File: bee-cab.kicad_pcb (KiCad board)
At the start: 2 copper layers, 29 x 53.3 mm, 38 parts, among them J1 Conn_01x02_Male, J10 Conn_01x01, J11 Conn_02x01, J12 Conn_02x01, J13 Conn_01x02, J14 Conn_01x02, J15 Conn_01x02, J16 Conn_01x02, J17 Conn_01x03, J18 Conn_01x02, J19 Conn_01x02, J2 Conn_01x02_Male, J3 Conn_01x02_Male, J4 Conn_01x02_Male, J5 Conn_01x03, J6 Conn_02x03_Odd_Even, J7 Conn_02x01, J8 Conn_01x02, J9 Conn_01x02

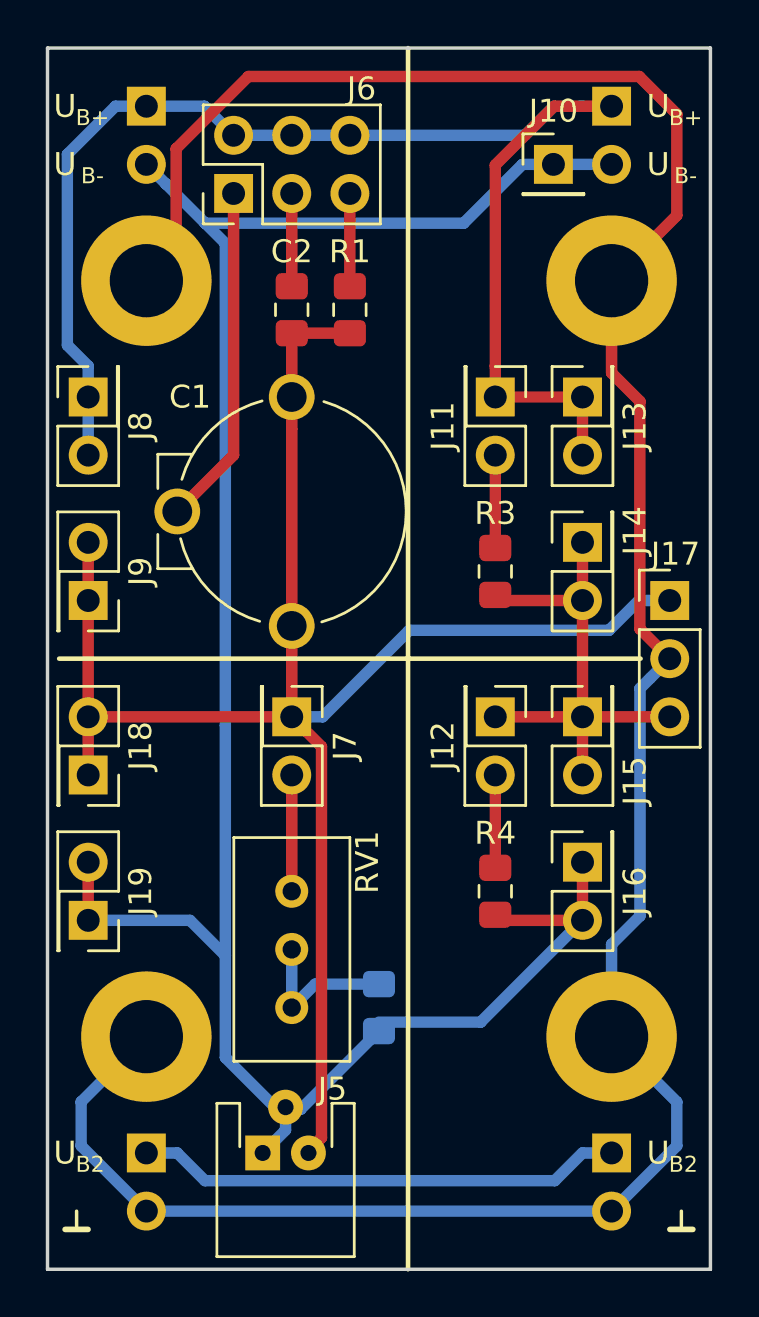
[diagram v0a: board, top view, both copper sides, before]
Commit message: Add text and logos.
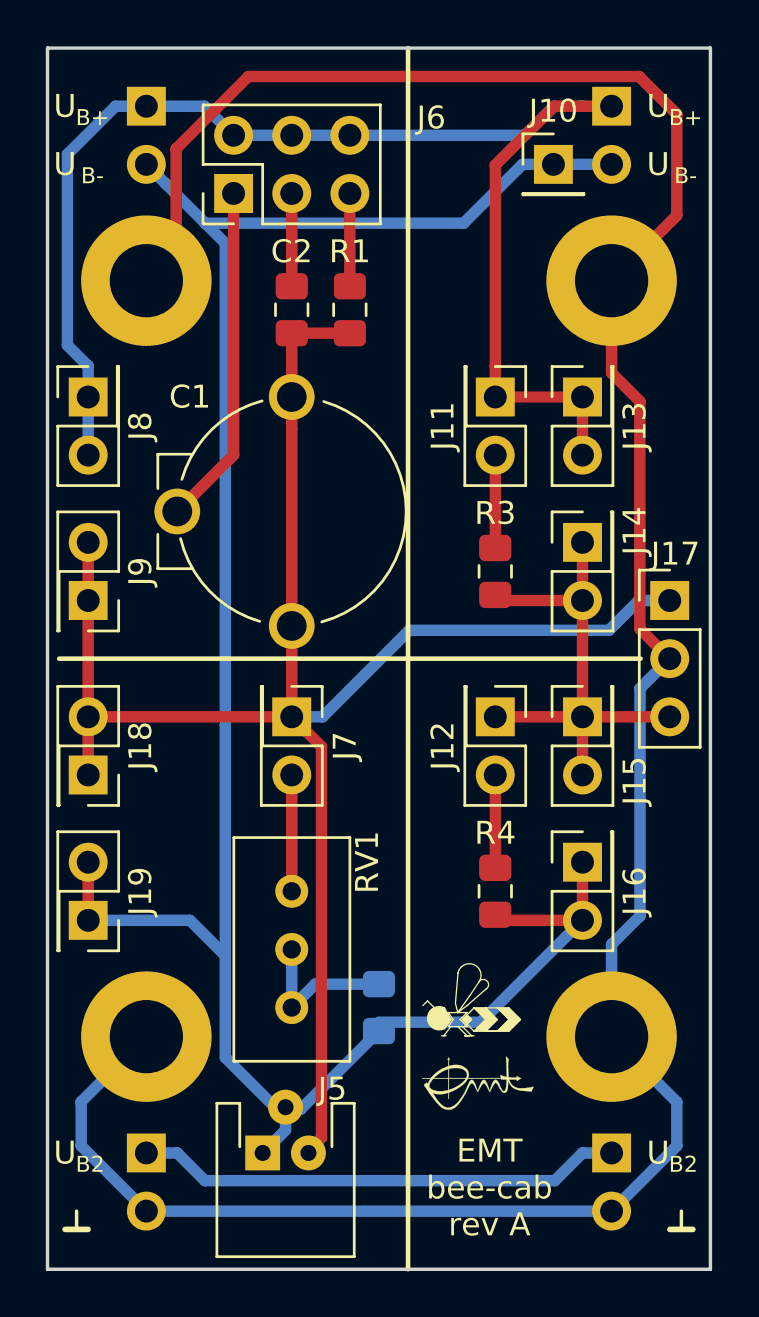
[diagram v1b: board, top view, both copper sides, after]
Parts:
- added H13: Silkscreen_Label, Symbol-emt:EMT-Logo_5.1x2.5mm_Silkscreen, F.Cu at (93.2, 134.1)
- added H14: Silkscreen_Label, Symbol-emt:BEE-Logo_Silkscreen_small, F.Cu at (92.7, 131.3)
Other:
- board text added: "EMT bee-cab rev A"

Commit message: Add pinheader for AC supply.
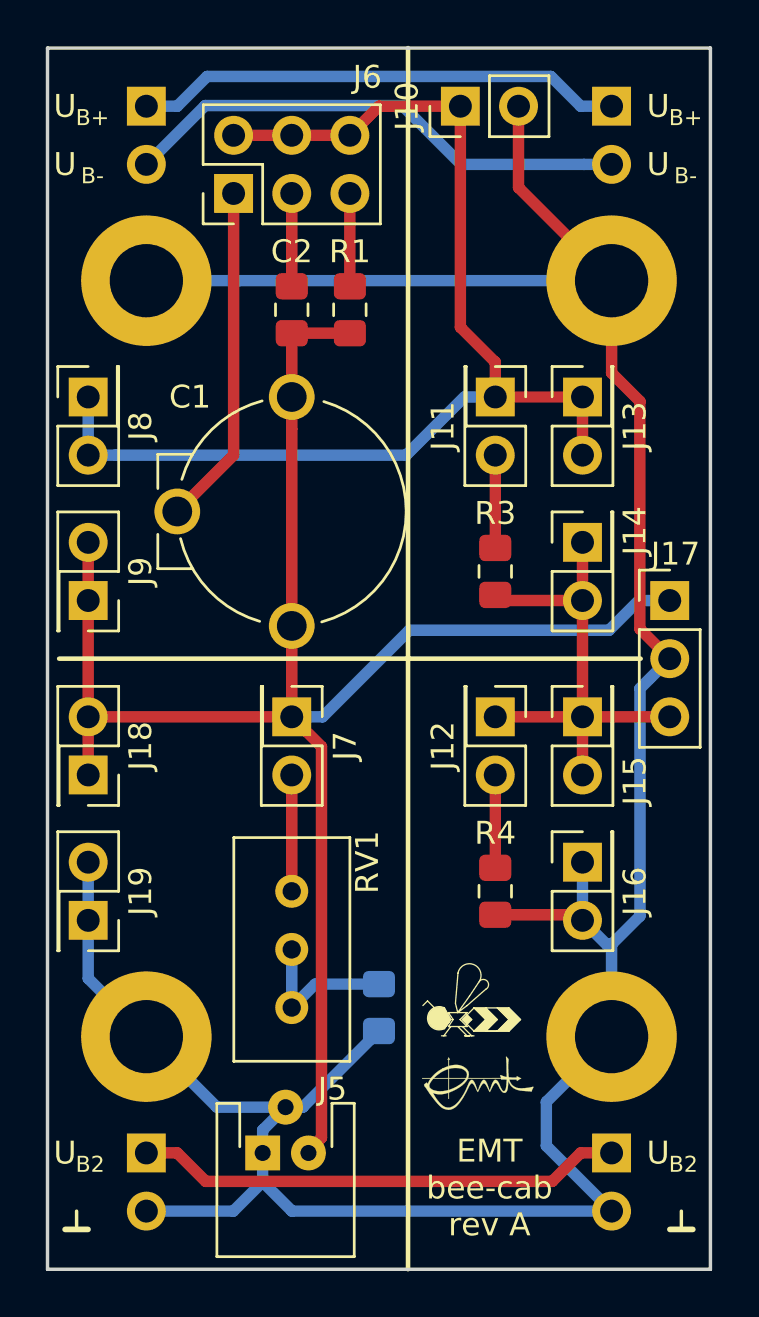
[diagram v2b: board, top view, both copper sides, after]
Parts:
- C1: value C_Variable -> 5,5-65p
- C2: value C -> 220n
- J10: value Conn_01x01 -> Conn_01x02_Male; footprint Connector_PinHeader_2.54mm:PinHeader_1x01_P2.54mm_Vertical -> Connector_PinHeader_2.54mm:PinHeader_1x02_P2.54mm_Vertical
- J5: value Conn_01x03 -> Molex
- R1: value R -> 1M
- R2: value R -> 910k
- R3, R4: value R -> 100k
- RV1: value R_POT -> 200k
- moved J10 4.79 mm to (92.5, 91.4), turned to 90 degrees
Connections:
- J10 pad 1: -15V -> VAC
- J11 pad 1: +15V -> VAC
- J13 pad 1: +15V -> VAC
- J13 pad 2: +15V -> VAC
- J16 pad 1: -15V -> GND
- J16 pad 2: -15V -> GND
- J19 pad 1: -15V -> GND
- J19 pad 2: -15V -> GND
- J5 pad 1: -15V -> GND
- J5 pad 2: -15V -> GND
- J6 pad 2: +15V -> VAC
- J6 pad 4: +15V -> VAC
- J6 pad 6: +15V -> VAC
- J8 pad 1: +15V -> VAC
- J8 pad 2: +15V -> VAC
- R2 pad 2: -15V -> GND
- R4 pad 2: -15V -> GND
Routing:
- net -15V: track 97.0 -> 22.4 mm
- net VAC: track 0.00 -> 51.5 mm
- net +15V: track 61.8 -> 21.4 mm
- net GND: track 114.0 -> 129.4 mm

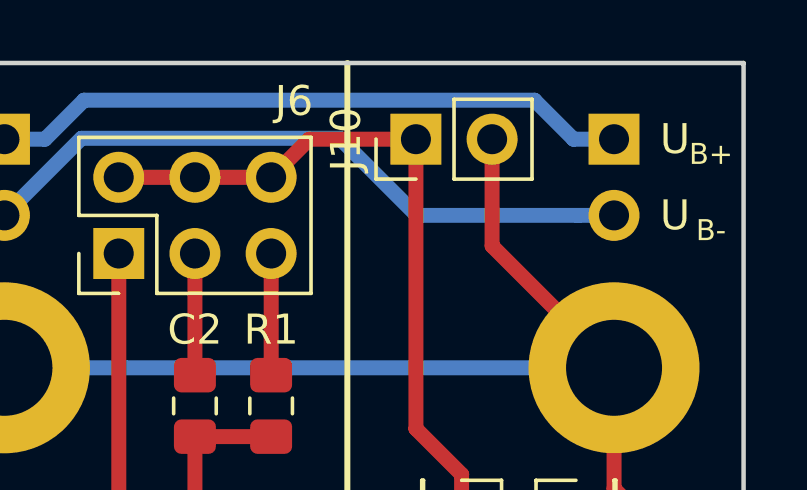
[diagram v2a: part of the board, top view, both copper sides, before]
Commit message: Add silkscreen labels.
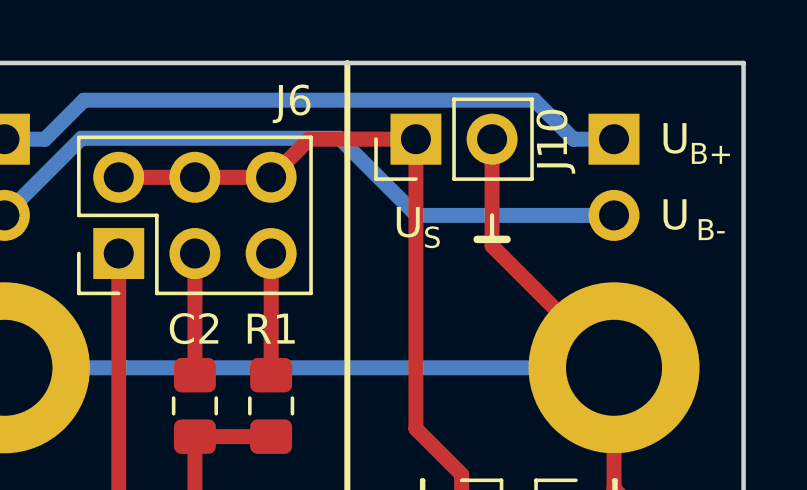
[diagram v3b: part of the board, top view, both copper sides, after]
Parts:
- added H15: Silkscreen_Label, Symbol-emt:Text_U_S_Silkscreen, F.Cu at (92.2, 94.2)
- added H16: Silkscreen_Label, Symbol-emt:Symbol_GND_Silkscreen, F.Cu at (95.0, 94.0)
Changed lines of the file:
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@@
     (tracks 98)
     (zones 0)
-    (modules 40)
+    (modules 42)
     (nets 15)
   )
@@
     (descr "Through hole straight pin header, 1x02, 2.54mm pitch, single row")
     (tags "Through hole pin header THT 1x02 2.54mm single row")
-    (fp_text reference J10 (at 0 -2.33 90) (layer F.SilkS)
+    (fp_text reference J10 (at 0 4.572 90) (layer F.SilkS)
       (effects (font (size 1 1) (thickness 0.15)))
     )
@@
     )
   )
+  (module Symbol-emt:Text_U_S_Silkscreen (layer F.Cu)
+    (at 92.202 94.234)
+    (descr "Voltage Label Betriebsspannung")
+    (tags "Voltage Label Betriebsspannung")
+    (attr virtual)
+    (fp_text reference H15 (at 0 1.65) (layer F.SilkS) hide
+      (effects (font (size 1 1) (thickness 0.15)))
+    )
+    (fp_text value Silkscreen_Label (at 0 -1.5) (layer F.Fab) hide
+      (effects (font (size 1 1) (thickness 0.15)))
+    )
+    (fp_text user U (at 0 0) (layer F.SilkS)
+      (effects (font (size 1 1) (thickness 0.15)))
+    )
+    (fp_text user S (at 0.8 0.5) (layer F.SilkS)
+      (effects (font (size 0.7 0.7) (thickness 0.1)))
+    )
+  )
+  (module Symbol-emt:Symbol_GND_Silkscreen (layer F.Cu)
+    (at 94.996 93.98)
+    (descr "Symbol GND")
+    (tags "Symbol GND")
+    (attr virtual)
+    (fp_text reference H16 (at 0 1.6) (layer F.SilkS) hide
+      (effects (font (size 1 1) (thickness 0.15)))
+    )
+    (fp_text value Silkscreen_Label (at 0 -0.75) (layer F.Fab) hide
+      (effects (font (size 1 1) (thickness 0.15)))
+    )
+    (fp_line (start -0.5 0.8) (end 0.5 0.8) (layer F.SilkS) (width 0.25))
+    (fp_line (start 0 0.8) (end 0 0) (layer F.SilkS) (width 0.15))
+  )
   (gr_text "EMT\nbee-cab\nrev A" (at 93.726 138.684) (layer F.SilkS)

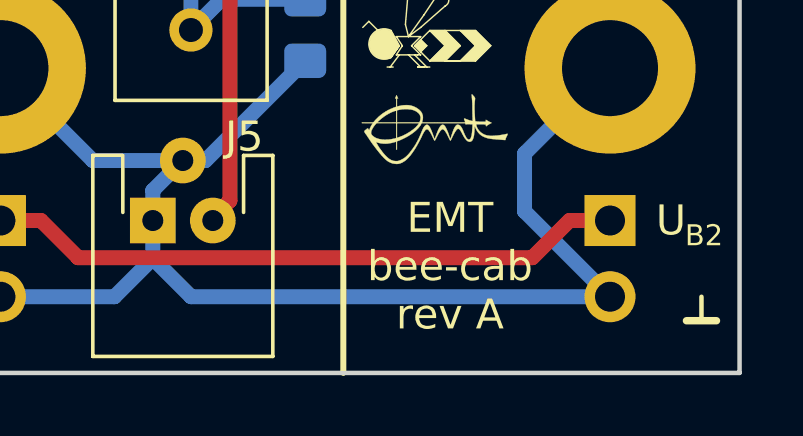
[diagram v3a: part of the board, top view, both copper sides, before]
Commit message: Increase revision label to B.
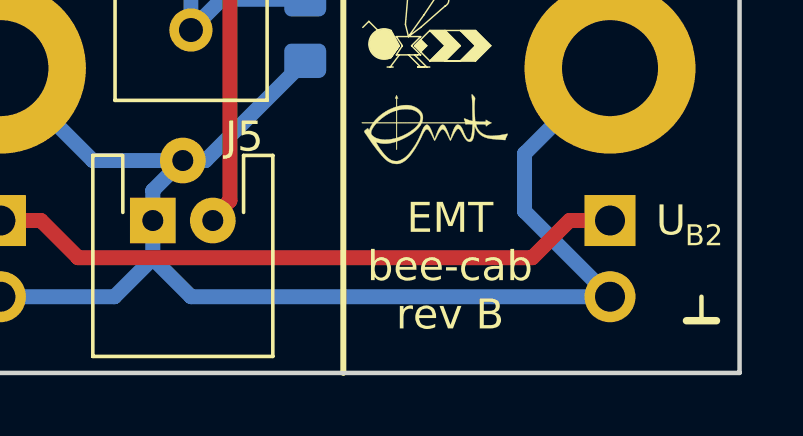
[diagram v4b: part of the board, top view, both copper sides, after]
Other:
- board text added: "EMT bee-cab rev B"
- board text removed: "EMT bee-cab rev A"
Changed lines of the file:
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@@
     (fp_line (start 0 0.8) (end 0 0) (layer F.SilkS) (width 0.15))
   )
-  (gr_text "EMT\nbee-cab\nrev A" (at 93.726 138.684) (layer F.SilkS)
+  (gr_text "EMT\nbee-cab\nrev B" (at 93.726 138.684) (layer F.SilkS)
     (effects (font (size 1 1) (thickness 0.15)))
   )

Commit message: Relabel as bee specific.
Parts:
- C1: footprint Capacitor_THT-emt:C_Trimmer_Vishay_D10mm_Vertical_HolePattern5mmx10mm -> Capacitor_THT-bee:C_Trimmer_Vishay_D10mm_Vertical_HolePattern5mmx10mm
- H1, H2: footprint Symbol-emt:Text_U_B+_Silkscreen -> Symbol-bee:Text_U_B+_Silkscreen
- H13: footprint Symbol-emt:EMT-Logo_5.1x2.5mm_Silkscreen -> Symbol-bee:EMT-Logo_5.1x2.5mm_Silkscreen
- H14: footprint Symbol-emt:BEE-Logo_Silkscreen_small -> Symbol-bee:BEE-Logo_Silkscreen_small
- H15: footprint Symbol-emt:Text_U_S_Silkscreen -> Symbol-bee:Text_U_S_Silkscreen
- H16, H7, H8: footprint Symbol-emt:Symbol_GND_Silkscreen -> Symbol-bee:Symbol_GND_Silkscreen
- H3, H4: footprint Symbol-emt:Text_U_B-_Silkscreen -> Symbol-bee:Text_U_B-_Silkscreen
- H5, H6: footprint Symbol-emt:Text_U_B2_Silkscreen -> Symbol-bee:Text_U_B2_Silkscreen
- J5: footprint Connector_Molex-emt:Molex_Easy-On_528070310_1x03_P1.0mm_Horizontal -> Connector_Molex-bee:Molex_Easy-On_528070310_1x03_P1.0mm_Horizontal
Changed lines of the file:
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@@
     )
   )
-  (module Capacitor_THT-emt:C_Trimmer_Vishay_D10mm_Vertical_HolePattern5mmx10mm (layer F.Cu)
+  (module Capacitor_THT-bee:C_Trimmer_Vishay_D10mm_Vertical_HolePattern5mmx10mm (layer F.Cu)
     (at 85.09 104.14 270)
     (descr http://www.vishay.com/docs/28528/bfc2808-10mm.pdf)
@@
     (pad 2 thru_hole circle (at 5 5 270) (size 2 2) (drill 1.3) (layers *.Cu *.Mask)
       (net 6 "Net-(C1-Pad2)"))
-    (model ${KICAD_3DMOD_EMT}/Capacitor_THT-emt.3dshapes/C_Trimmer_Vishay_D10mm_Vertical_HolePattern5mmx10mm.wrl
+    (model ${KICAD_3DMOD_BEE}/Capacitor_THT-bee.3dshapes/C_Trimmer_Vishay_D10mm_Vertical_HolePattern5mmx10mm.wrl
       (at (xyz 0 0 0))
       (scale (xyz 1 1 1))
@@
     )
   )
-  (module Connector_Molex-emt:Molex_Easy-On_528070310_1x03_P1.0mm_Horizontal (layer F.Cu)
+  (module Connector_Molex-bee:Molex_Easy-On_528070310_1x03_P1.0mm_Horizontal (layer F.Cu)
     (at 83.82 137.16)
     (descr https://www.molex.com/pdm_docs/sd/528070310_sd.pdf)
@@
     (pad 3 thru_hole circle (at 2 0) (size 1.524 1.524) (drill 0.7) (layers *.Cu *.Mask)
       (net 5 "Net-(C1-Pad1)"))
-    (model ${KICAD_3DMOD_EMT}/Connector_Molex-emt.3dshapes/Molex_Easy-On_528070310_1x03_P1.0mm_Horizontal.wrl
+    (model ${KICAD_3DMOD_BEE}/Connector_Molex-bee.3dshapes/Molex_Easy-On_528070310_1x03_P1.0mm_Horizontal.wrl
       (at (xyz 0 0 0))
       (scale (xyz 1 1 1))
@@
     )
   )
-  (module Symbol-emt:Text_U_B+_Silkscreen (layer F.Cu)
+  (module Symbol-bee:Text_U_B+_Silkscreen (layer F.Cu)
     (at 75.184 91.44)
     (descr "Voltage Label Betriebsspannung")
@@
     )
   )
-  (module Symbol-emt:Text_U_B+_Silkscreen (layer F.Cu)
+  (module Symbol-bee:Text_U_B+_Silkscreen (layer F.Cu)
     (at 101.092 91.44)
     (descr "Voltage Label Betriebsspannung")
@@
     )
   )
-  (module Symbol-emt:Text_U_B-_Silkscreen (layer F.Cu)
+  (module Symbol-bee:Text_U_B-_Silkscreen (layer F.Cu)
     (at 75.184 93.98)
     (descr "Voltage Label Betriebsspannung")
@@
     )
   )
-  (module Symbol-emt:Text_U_B-_Silkscreen (layer F.Cu)
+  (module Symbol-bee:Text_U_B-_Silkscreen (layer F.Cu)
     (at 101.092 93.98)
     (descr "Voltage Label Betriebsspannung")
@@
     )
   )
-  (module Symbol-emt:Text_U_B2_Silkscreen (layer F.Cu)
+  (module Symbol-bee:Text_U_B2_Silkscreen (layer F.Cu)
     (at 75.184 137.16)
     (descr "Voltage Label Betriebsspannung")
@@
     )
   )
-  (module Symbol-emt:Text_U_B2_Silkscreen (layer F.Cu)
+  (module Symbol-bee:Text_U_B2_Silkscreen (layer F.Cu)
     (at 101.092 137.16)
     (descr "Voltage Label Betriebsspannung")
@@
     )
   )
-  (module Symbol-emt:Symbol_GND_Silkscreen (layer F.Cu)
+  (module Symbol-bee:Symbol_GND_Silkscreen (layer F.Cu)
     (at 75.692 139.7)
     (descr "Symbol GND")
@@
     (fp_line (start -0.5 0.8) (end 0.5 0.8) (layer F.SilkS) (width 0.25))
   )
-  (module Symbol-emt:Symbol_GND_Silkscreen (layer F.Cu)
+  (module Symbol-bee:Symbol_GND_Silkscreen (layer F.Cu)
     (at 102.108 139.7)
     (descr "Symbol GND")
@@
       (net 3 GND))
   )
-  (module Symbol-emt:EMT-Logo_5.1x2.5mm_Silkscreen (layer F.Cu)
+  (module Symbol-bee:EMT-Logo_5.1x2.5mm_Silkscreen (layer F.Cu)
     (at 93.218 134.112)
     (descr EMT-Logo)
@@
       (xy 1.243014 -1.158797)) (layer F.SilkS) (width 0.01))
   )
-  (module Symbol-emt:BEE-Logo_Silkscreen_small (layer F.Cu)
+  (module Symbol-bee:BEE-Logo_Silkscreen_small (layer F.Cu)
     (at 92.71 131.318)
     (descr BEE-Logo)
@@
     )
   )
-  (module Symbol-emt:Text_U_S_Silkscreen (layer F.Cu)
+  (module Symbol-bee:Text_U_S_Silkscreen (layer F.Cu)
     (at 92.202 94.234)
     (descr "Voltage Label Betriebsspannung")
@@
     )
   )
-  (module Symbol-emt:Symbol_GND_Silkscreen (layer F.Cu)
+  (module Symbol-bee:Symbol_GND_Silkscreen (layer F.Cu)
     (at 94.996 93.98)
     (descr "Symbol GND")
